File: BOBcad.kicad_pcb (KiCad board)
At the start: 4 copper layers, 100 x 68 mm, 26 parts, among them J1 CN3791, J10 Programming, J12 EN, J2 JTAG, J3 DS18B20, J4 BME280, J6 Load Cell, J7 DS3231, Q1 S8050, Q2 S8050, U1 NCP380, U2 HX711, U3 WIPY, U4 ESP32_DevKit_V1

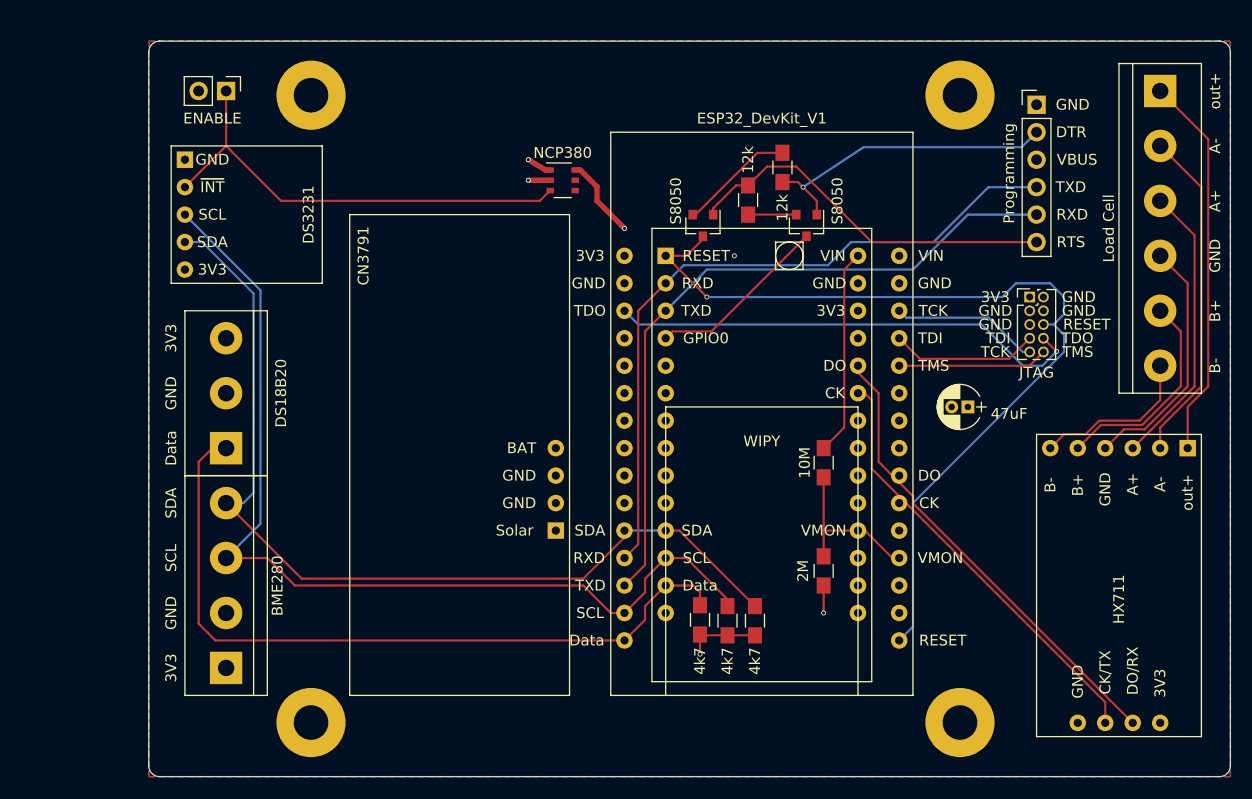
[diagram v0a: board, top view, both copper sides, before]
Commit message: v1.0.2
Added solar voltage monitoring
Modified power plane
Added two more capacitors for 3v3 lines to sensors
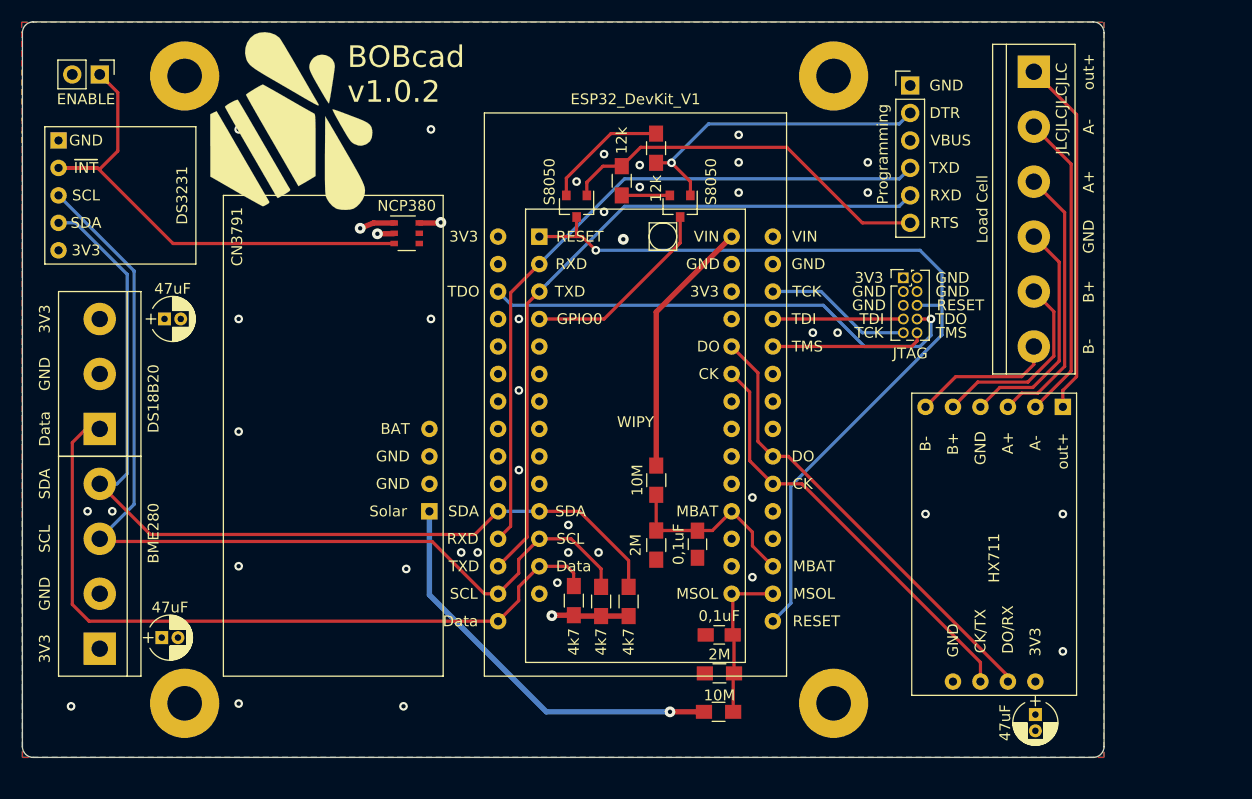
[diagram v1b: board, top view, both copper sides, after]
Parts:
- added C1: 0,1uF, Capacitors_SMD:C_0805_HandSoldering, F.Cu at (154.0, 109.0)
- added C3: 0,1uF, Capacitors_SMD:C_0805_HandSoldering, F.Cu at (156.1, 117.4)
- added C4: 47uF, Capacitors_ThroughHole:CP_Radial_D4.0mm_P1.50mm, F.Cu at (104.5, 117.6)
- added C5: 47uF, Capacitors_ThroughHole:CP_Radial_D4.0mm_P1.50mm, F.Cu at (104.8, 88.1)
- added G***: LOGO, BOBcad:BOB_logo, F.Cu at (116.4, 69.9)
- added R8: 10M, Resistors_SMD:R_0805_HandSoldering, F.Cu at (156.0, 124.5)
- added R9: 2M, Resistors_SMD:R_0805_HandSoldering, F.Cu at (156.1, 120.9)
- moved C2 29.1 mm to (185.3, 124.7), turned to 270 degrees
- moved R2 15.7 mm to (150.2, 109.1)
- moved R1 15.6 mm to (150.2, 103.1)
- moved U1 15.2 mm to (127.2, 80.2)
- moved U2 12.2 mm to (187.8, 96.3)
- moved J7 11.8 mm to (95.0, 71.6)
- moved H1 11.8 mm to (106.6, 65.7)
- moved H2 11.8 mm to (166.6, 65.7)
- moved H3 11.8 mm to (106.6, 123.7)
- moved H4 11.8 mm to (166.6, 123.7)
- moved J1 11.8 mm to (130.5, 76.7)
- moved J10 11.8 mm to (173.7, 66.6)
- moved J2 11.8 mm to (173.1, 84.3)
- moved J3 11.8 mm to (98.8, 98.3)
- moved J4 11.8 mm to (98.8, 118.6)
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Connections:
- J1 pad 1: (no net) -> /Solar
- U3 pad 15: (no net) -> /GPIO36
- U4 pad 2: (no net) -> /GPIO36
- U4 pad 3: (no net) -> /GPIO39
- U4 pad 4: /GPIO39 -> (no net)
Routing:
- net /3V3: track 216.5 -> 7.82 mm
- net /Solar: track 0.00 -> 37.6 mm, vias 0 -> 1
- net /GPIO36: track 0.00 -> 14.9 mm
- net /BAT: track 31.1 -> 24.4 mm
- net /~INT: track 42.9 -> 47.6 mm
- net /3.5-5.5V: track 69.5 -> 73.7 mm
- net GND: track 4.55 -> 1.57 mm, vias 3 -> 40
- net /GPIO39: track 15.3 -> 18.3 mm
- net Net-(J6-Pad1): track 35.7 -> 33.1 mm
- net Net-(J6-Pad2): track 31.1 -> 28.7 mm
- net /RESET: track 84.0 -> 82.0 mm
- net /SCL: track 92.0 -> 90.1 mm
- net Net-(J6-Pad6): track 15.2 -> 13.3 mm
- net Net-(J6-Pad5): track 19.7 -> 18.0 mm
- net Net-(J6-Pad4): track 23.1 -> 21.5 mm
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- added copper zone on PWR, net /3V3
- removed copper zone on PWR, net GND
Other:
- net class Default: trace_width 0.2 -> 0.3; via_dia 0.45 -> 0.8; via_drill 0.3 -> 0.4
- net class Power added: clearance 0.2, trace_width 0.5, via_dia 1, via_drill 0.4
- board text added: "BOBcad v1.0.2"
- board text added: "JLCJLCJLCJLC"
